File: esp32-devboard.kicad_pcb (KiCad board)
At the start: 4 copper layers, 40.4 x 36.3 mm, 41 parts, among them J1 USB_C_Receptacle_USB2.0_16P, J2 CA, J3 CB, SW1 BOOT, SW2 RST, SW3 FLIP, SW4 FLOP, U1 ESP32-C6-MINI-1/U, U2 AMS1117-3.3

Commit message: almost done with layout
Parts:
- C1, D2, D3, D4: moved to B.Cu
- R4, R8, R9: moved to F.Cu
- moved D3 126.7 mm to (237.0, 103.0), turned to 180 degrees
- moved J2 122.3 mm to (248.5, 86.0)
- moved D2 122.0 mm to (232.8, 103.0)
- moved R1 120.6 mm to (236.0, 110.2)
- moved D4 120.3 mm to (228.0, 105.8)
- moved R2 117.7 mm to (232.8, 110.2), turned to 180 degrees
- moved R6 112.6 mm to (229.8, 93.5), turned to 180 degrees
- moved D7 108.0 mm to (236.2, 97.5), turned to 90 degrees
- moved R10 107.2 mm to (234.5, 91.2), turned to 90 degrees
- moved C1 101.0 mm to (244.2, 106.2)
- moved J3 100.1 mm to (220.5, 86.0)
- moved R8 87.3 mm to (233.5, 97.5)
- moved R9 83.6 mm to (231.5, 97.5)
- moved R4 79.9 mm to (229.5, 97.5)
- moved TP2 19.6 mm to (281.8, 91.8), turned to 180 degrees
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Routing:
- net /ESP32/USB_D-: track 2.51 -> 13.4 mm
- net /ESP32/USB_D+: track 2.38 -> 13.3 mm
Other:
- outline, holes or cut-outs redrawn
- board text added: "EVIL ESP32"
- board text added: "Ravi Shah 2025"

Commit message: layout kinda done
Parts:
- removed TP1: 5V, TestPoint:TestPoint_Pad_D1.0mm
- C2, C3, C4, C5: moved to B.Cu
- R3, R7: moved to F.Cu
- moved TP3 146.0 mm to (131.8, 89.8)
- moved R3 128.7 mm to (137.6, 108.2), turned to 90 degrees
- moved R7 126.6 mm to (139.5, 108.2), turned to 90 degrees
- moved TP2 114.5 mm to (167.2, 89.8)
- moved C2 114.3 mm to (155.0, 106.8), turned to 90 degrees
- moved C3 110.6 mm to (159.2, 111.5)
- moved C4 110.1 mm to (160.5, 97.0)
- moved C5 109.9 mm to (160.5, 98.8)
- moved C12 86.9 mm to (152.0, 105.2), turned to 0 degrees
- moved R5 86.1 mm to (158.0, 94.0), turned to 0 degrees
- moved C8 85.1 mm to (157.2, 97.0)
- moved C10 85.1 mm to (157.2, 90.8)
- moved C11 85.1 mm to (145.0, 106.0)
- moved C6 85.1 mm to (137.8, 101.5)
- moved C9 85.1 mm to (159.0, 90.8)
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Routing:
- removed copper zone on F.Cu, net /Power/+5V

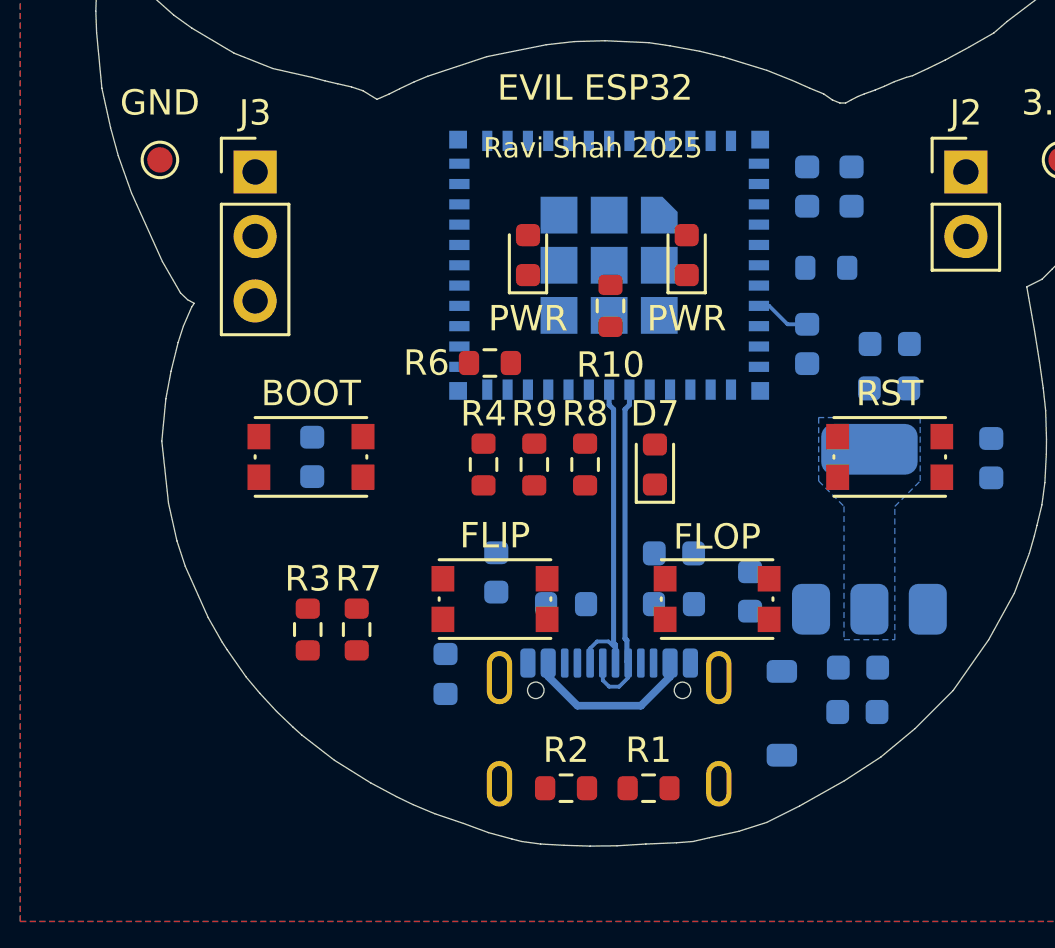
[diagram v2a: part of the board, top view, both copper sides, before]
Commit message: USB routing
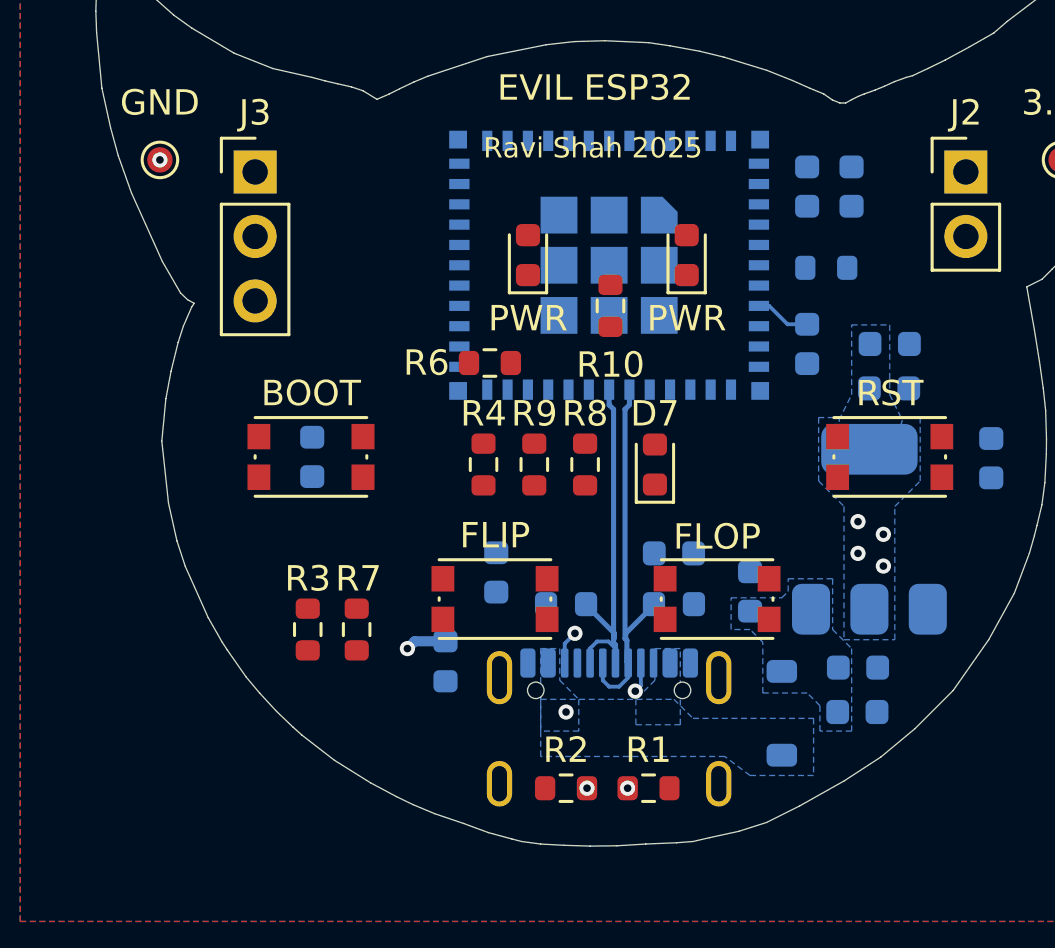
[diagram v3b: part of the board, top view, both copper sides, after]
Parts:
- moved D4 0.50 mm to (143.0, 109.5)
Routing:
- net /USB/CC2: track 0.00 -> 7.63 mm, vias 0 -> 2
- net /USB/CC1: track 0.00 -> 5.15 mm, vias 0 -> 2
- net /USB/VBUSB: track 6.81 -> 9.13 mm, vias 0 -> 2
- net /ESP32/USB_D+: track 13.3 -> 15.1 mm
- net /ESP32/USB_D-: track 13.4 -> 15.2 mm
- net GND: vias 0 -> 1
- net +3.3V: vias 0 -> 4
- added copper zone on B.Cu, net /Power/+5V
- added copper zone on B.Cu, net /USB/VBUSB

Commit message: initial routing
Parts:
- moved C12 1.25 mm to (153.0, 104.5), turned to 90 degrees
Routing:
- net Net-(D6-A): track 0.00 -> 27.7 mm, vias 0 -> 3
- net Net-(D5-A): track 0.00 -> 21.4 mm, vias 0 -> 3
- net /Devices/FLOP: track 0.00 -> 19.6 mm, vias 0 -> 3
- net /Devices/RST: track 2.20 -> 19.0 mm, vias 0 -> 3
- net /Devices/FLIP: track 0.00 -> 16.6 mm, vias 0 -> 2
- net /ESP32/GPIO_0: track 0.00 -> 16.5 mm, vias 0 -> 2
- net GND: track 0.00 -> 15.4 mm, vias 1 -> 38
- net /ESP32/GPIO_1: track 0.00 -> 13.9 mm, vias 0 -> 2
- net /Devices/BOOT: track 0.00 -> 13.2 mm, vias 0 -> 4
- net /ESP32/GPIO_23: track 0.00 -> 9.90 mm, vias 0 -> 1
- net /ESP32/GPIO_22: track 0.00 -> 9.18 mm, vias 0 -> 1
- net /ESP32/GPIO_21: track 0.00 -> 8.46 mm, vias 0 -> 1
- net /Devices/LED_0: track 0.00 -> 7.06 mm, vias 0 -> 1
- net Net-(D7-A): track 0.00 -> 7.01 mm, vias 0 -> 2
- net +3.3V: track 0.00 -> 1.93 mm, vias 4 -> 28
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
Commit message: stupid dumb drc
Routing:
- net GND: vias 38 -> 37
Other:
- board text added: "put some cool silkscreen on here...."

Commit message: add BOM
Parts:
- moved C3 1.75 mm to (159.2, 109.8)
- moved C1 1.75 mm to (159.2, 111.5)
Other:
- board text added: "0"
- board text added: "1"
- board text added: "21"
- board text added: "22"
- board text added: "23"
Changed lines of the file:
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@@
 	(footprint "Capacitor_SMD:C_0603_1608Metric"
 		(layer "B.Cu")
-		(at 159.25 109.75)
+		(at 159.25 111.5)
 		(descr "Capacitor SMD 0603 (1608 Metric), square (rectangular) end terminal, IPC_7351 nominal, (Body size source: IPC-SM-782 page 76, https://www.pcb-3d.com/wordpress/wp-content/uploads/ipc-sm-782a_amendment_1_and_2.pdf), generated with kicad-footprint-generator")
 		(tags "capacitor")
 		(property "Reference" "C1"
-			(at 2.25 -0.25 0)
+			(at 2 -0.5 90)
 			(layer "B.SilkS")
 			(effects
 				(font
-					(size 1 1)
-					(thickness 0.15)
+					(size 0.8 0.8)
+					(thickness 0.12)
 				)
 				(justify mirror)
@@
 	(footprint "Capacitor_SMD:C_0603_1608Metric"
 		(layer "B.Cu")
-		(at 159.225 111.5)
+		(at 159.25 109.75)
 		(descr "Capacitor SMD 0603 (1608 Metric), square (rectangular) end terminal, IPC_7351 nominal, (Body size source: IPC-SM-782 page 76, https://www.pcb-3d.com/wordpress/wp-content/uploads/ipc-sm-782a_amendment_1_and_2.pdf), generated with kicad-footprint-generator")
 		(tags "capacitor")
 		(property "Reference" "C3"
-			(at 2.025 -0.5 90)
+			(at 2.25 -0.25 180)
 			(layer "B.SilkS")
 			(effects
@@
 		)
 	)
+	(gr_text "21"
+		(at 137.25 96 0)
+		(layer "F.SilkS" knockout)
+		(effects
+			(font
+				(size 1 1)
+				(thickness 0.15)
+			)
+			(justify left bottom)
+		)
+	)
+	(gr_text "1"
+		(at 160.5 93.25 0)
+		(layer "F.SilkS" knockout)
+		(effects
+			(font
+				(size 1 1)
+				(thickness 0.15)
+			)
+			(justify left bottom)
+		)
+	)
 	(gr_text "EVIL ESP32"
 		(at 145.035988 87.5 0)
 		(layer "F.SilkS" knockout)
 		(effects
+			(font
+				(size 1 1)
+				(thickness 0.15)
+			)
+			(justify left bottom)
+		)
+	)
+	(gr_text "23"
+		(at 137.25 90.75 0)
+		(layer "F.SilkS" knockout)
+		(effects
+			(font
+				(size 1 1)
+				(thickness 0.15)
+			)
+			(justify left bottom)
+		)
+	)
+	(gr_text "22"
+		(at 137.25 93.25 0)
+		(layer "F.SilkS" knockout)
+		(effects
+			(font
+				(size 1 1)
+				(thickness 0.15)
+			)
+			(justify left bottom)
+		)
+	)
+	(gr_text "0"
+		(at 160.5 91 0)
+		(layer "F.SilkS" knockout)
+		(effects

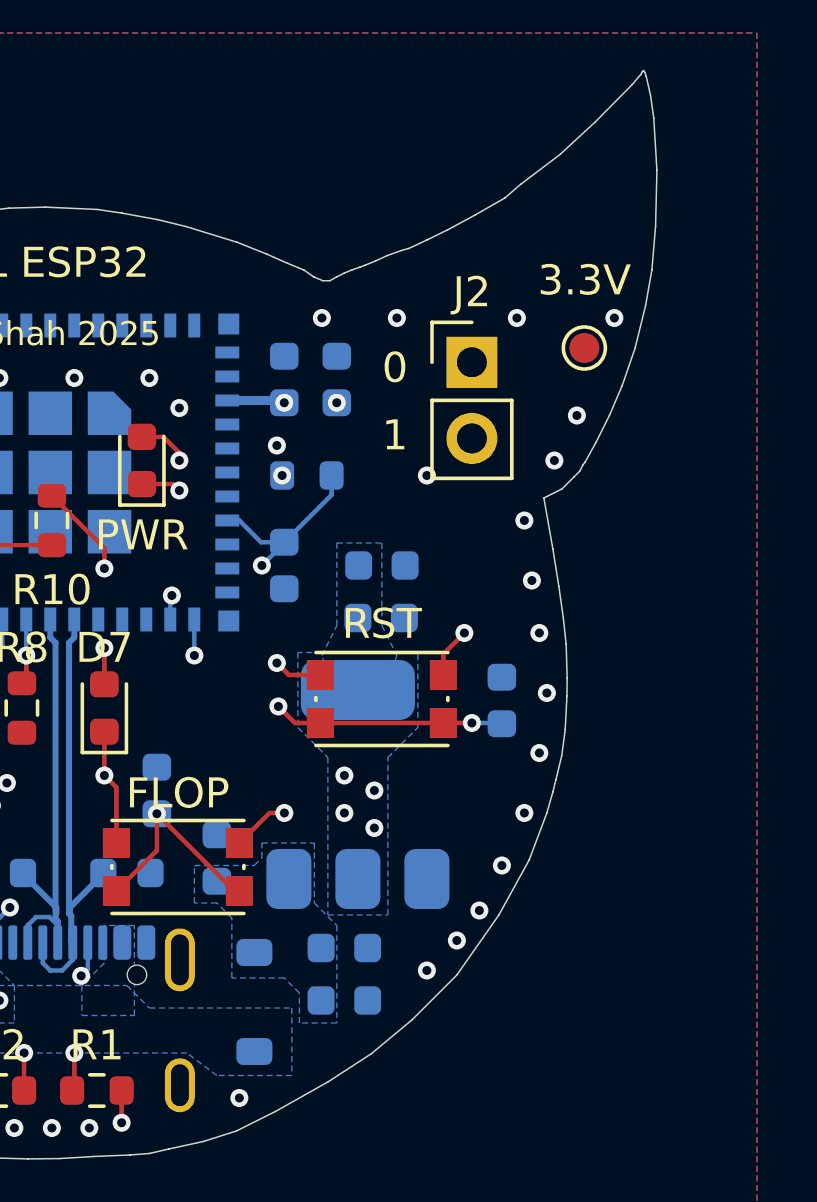
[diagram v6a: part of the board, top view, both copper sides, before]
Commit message: readme, mounting holes, minor silk changes
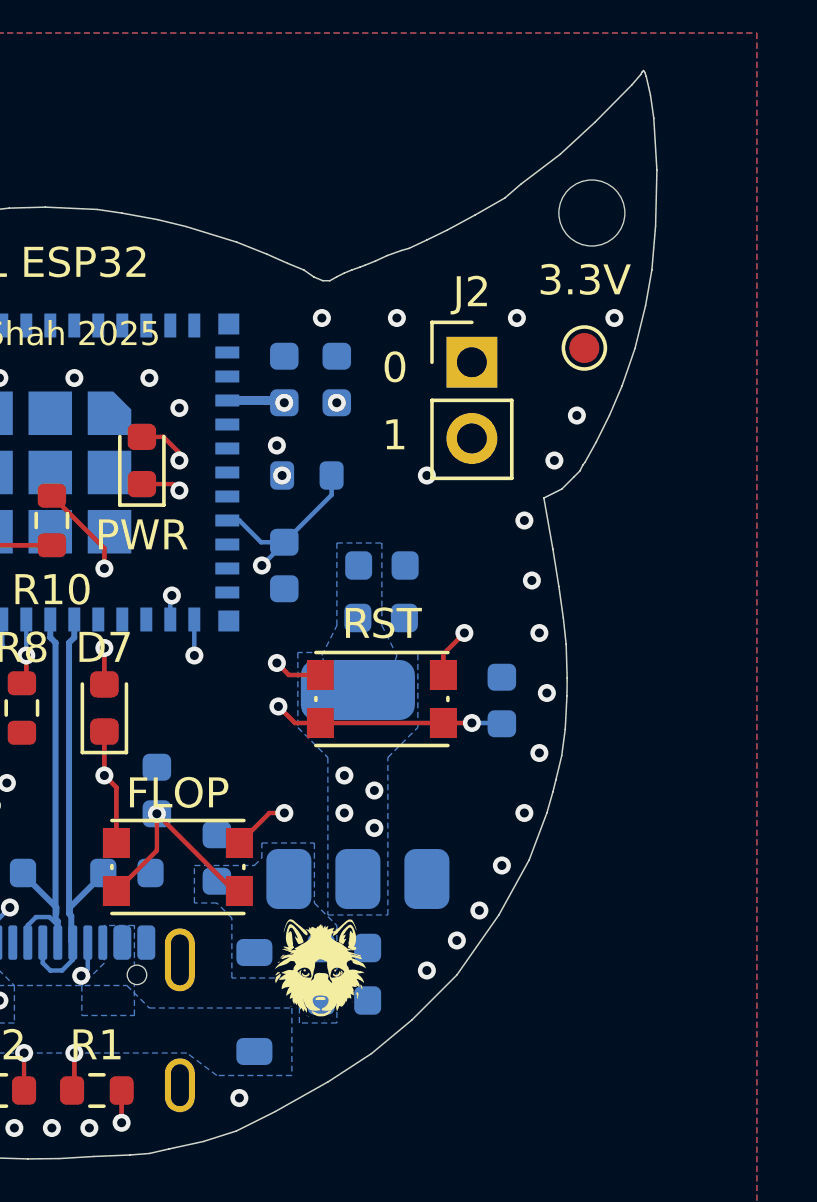
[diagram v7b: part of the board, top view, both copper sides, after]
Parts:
- added G***: LOGO, LOGO, F.Cu at (158.5, 110.5)
- added H1: MountingHole, MountingHole:MountingHole_2.2mm_M2, F.Cu at (167.5, 85.2)

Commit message: add cool silkscreen
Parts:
- added G***: LOGO, LOGO, F.Cu at (159.2, 109.2)
- added G***: LOGO, LOGO, F.Cu at (159.2, 95.5)
- added G***: LOGO, LOGO, F.Cu at (142.2, 91.8)
- added G***: LOGO, LOGO, B.Cu at (130.3, 81.7)
- added G***: LOGO, LOGO, B.Cu at (138.5, 96.2)
- added G***: LOGO, LOGO, B.Cu at (141.2, 102.8)
- added G***: LOGO, LOGO, B.Cu at (139.0, 108.5)
- added G***: LOGO, LOGO, B.Cu at (166.0, 88.2)
- moved G*** 16.5 mm to (142.0, 111.8)
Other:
- board text removed: "put some cool silkscreen on here...."
